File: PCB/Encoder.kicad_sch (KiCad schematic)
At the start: 1 part, among them U5 AS5047P-ATSM_C962063

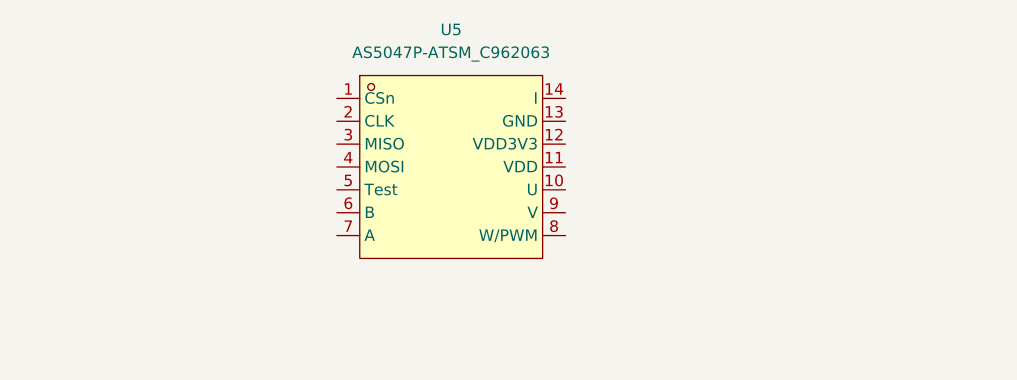
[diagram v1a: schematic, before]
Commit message: Added bldc driver
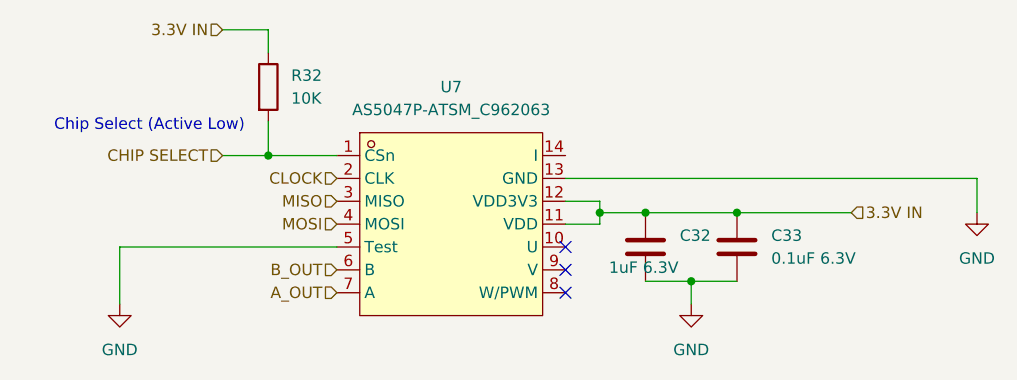
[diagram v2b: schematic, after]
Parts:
- removed U5: AS5047P-ATSM_C962063, easyeda2kicad:TSSOP-14_L5.0-W4.4-P0.65-LS6.4-BL, symbol easyeda2kicad:AS5047P-ATSM_C962063
- added C32: 1uF 6.3V, Capacitor_SMD:C_0603_1608Metric_Pad1.08x0.95mm_HandSolder, symbol Device:C
- added C33: 0.1uF 6.3V, Capacitor_SMD:C_0603_1608Metric_Pad1.08x0.95mm_HandSolder, symbol Device:C
- added R32: 10K, Resistor_SMD:R_0603_1608Metric_Pad0.98x0.95mm_HandSolder, symbol Device:R
- added U7: AS5047P-ATSM_C962063, easyeda2kicad:TSSOP-14_L5.0-W4.4-P0.65-LS6.4-BL, symbol easyeda2kicad:AS5047P-ATSM_C962063
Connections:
- new net 3.3V IN: C32.1, C33.1, R32.1, U7.11 (VDD), U7.12 (VDD3V3)
- new net A_OUT: U7.7 (A)
- new net B_OUT: U7.6 (B)
- new net CHIP SELECT: R32.2, U7.1 (CSn)
- new net CLOCK: U7.2 (CLK)
- new net GND: C32.2, C33.2, U7.13 (GND), U7.5 (Test)
- new net MISO: U7.3 (MISO)
- new net MOSI: U7.4 (MOSI)
- no-connect marks 0 -> 3
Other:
- note added: "Chip Select (Active Low)"
